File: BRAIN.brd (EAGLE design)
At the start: 125 x 60 mm, 60 parts, among them IC1 ATMEGA328P, IC2 EUP3476SO08T, IC3 RXB1, IC4 TX-C1FLAT, J1 DC_2_1MM, Q1 RJU003N03 N-MOSFET, Q2 RJU003N03 N-MOSFET, Q3 RJU003N03 N-MOSFET, X1 16MHz HC49S

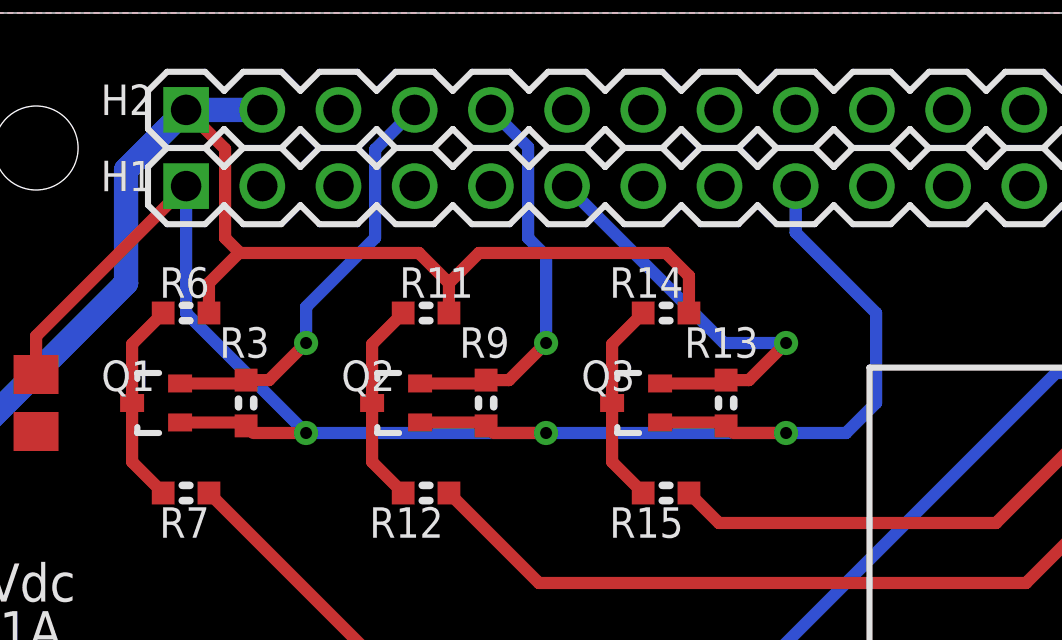
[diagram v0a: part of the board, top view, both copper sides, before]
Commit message: Moved Arduino RESET line from RTS to GPIO4 for manual control
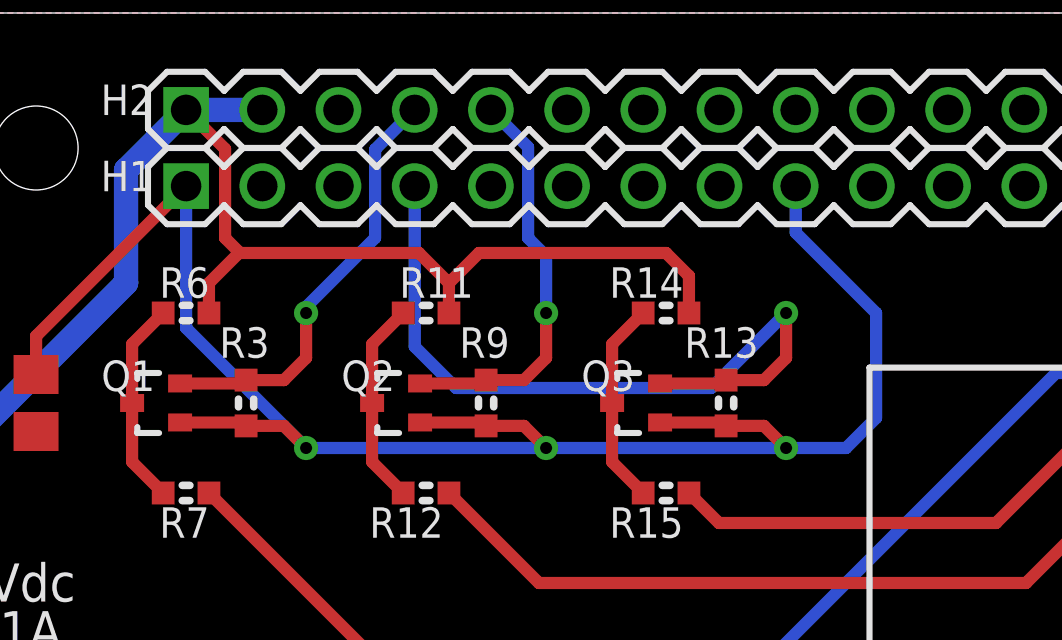
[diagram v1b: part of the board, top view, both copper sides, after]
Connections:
- net GPIO4: now also Q3.2, R13.2
- net PI_RTS: no longer Q3.2, R13.2
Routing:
- net GPIO4: track 0.00 -> 25.5 mm, vias 0 -> 1
- net PI_RTS: track 14.3 -> 0.00 mm, vias 1 -> 0
- net 3.3V: track 59.2 -> 60.8 mm
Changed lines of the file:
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@@
 <layer number="14" name="Route14" color="1" fill="6" visible="no" active="no"/>
 <layer number="15" name="Route15" color="4" fill="6" visible="no" active="no"/>
-<layer number="16" name="Bottom" color="1" fill="1" visible="no" active="yes"/>
+<layer number="16" name="Bottom" color="1" fill="1" visible="yes" active="yes"/>
 <layer number="17" name="Pads" color="2" fill="1" visible="yes" active="yes"/>
-<layer number="18" name="Vias" color="2" fill="1" visible="no" active="yes"/>
+<layer number="18" name="Vias" color="2" fill="1" visible="yes" active="yes"/>
 <layer number="19" name="Unrouted" color="12" fill="1" visible="yes" active="yes"/>
 <layer number="20" name="Dimension" color="15" fill="1" visible="yes" active="yes"/>
@@
 <wire x1="22.8" y1="47.65" x2="25" y2="47.65" width="0.4064" layer="1"/>
 <wire x1="25" y1="47.65" x2="25" y2="47.762" width="0.4064" layer="1"/>
-<wire x1="25" y1="47.762" x2="25.762" y2="47.762" width="0.4064" layer="1"/>
-<wire x1="25.762" y1="47.762" x2="27" y2="49" width="0.4064" layer="1"/>
-<via x="27" y="49" extent="1-16" drill="0.4"/>
+<wire x1="25" y1="47.762" x2="26.262" y2="47.762" width="0.4064" layer="1"/>
+<wire x1="26.262" y1="47.762" x2="27" y2="48.5" width="0.4064" layer="1"/>
+<wire x1="27" y1="48.5" x2="27" y2="50" width="0.4064" layer="1"/>
+<via x="27" y="50" extent="1-16" drill="0.4"/>
 <wire x1="30.62" y1="56.77" x2="29.3" y2="55.45" width="0.4064" layer="16"/>
 <wire x1="29.3" y1="55.45" x2="29.3" y2="52.5" width="0.4064" layer="16"/>
 <wire x1="29.3" y1="52.5" x2="27" y2="50.2" width="0.4064" layer="16"/>
-<wire x1="27" y1="50.2" x2="27" y2="49" width="0.4064" layer="16"/>
+<wire x1="27" y1="50.2" x2="27" y2="50" width="0.4064" layer="16"/>
 </signal>
 <signal name="3.3V">
@@
 <contactref element="H1" pad="1"/>
 <contactref element="H1" pad="9"/>
-<wire x1="25" y1="46.238" x2="25.238" y2="46" width="0.3048" layer="1"/>
-<wire x1="25.238" y1="46" x2="27" y2="46" width="0.4064" layer="1"/>
-<via x="27" y="46" extent="1-16" drill="0.4"/>
-<wire x1="27" y1="46" x2="35" y2="46" width="0.4064" layer="16"/>
-<via x="35" y="46" extent="1-16" drill="0.4"/>
-<wire x1="33" y1="46.238" x2="33.238" y2="46" width="0.3048" layer="1"/>
-<wire x1="33.238" y1="46" x2="35" y2="46" width="0.4064" layer="1"/>
-<wire x1="35" y1="46" x2="43" y2="46" width="0.4064" layer="16"/>
-<via x="43" y="46" extent="1-16" drill="0.4"/>
-<wire x1="43" y1="46" x2="41.238" y2="46" width="0.4064" layer="1"/>
-<wire x1="41.238" y1="46" x2="41" y2="46.238" width="0.3048" layer="1"/>
-<wire x1="23" y1="54.23" x2="23" y2="50" width="0.4064" layer="16"/>
-<wire x1="23" y1="50" x2="27" y2="46" width="0.4064" layer="16"/>
+<via x="27" y="45.5" extent="1-16" drill="0.4"/>
+<wire x1="27" y1="45.5" x2="35" y2="45.5" width="0.4064" layer="16"/>
+<via x="35" y="45.5" extent="1-16" drill="0.4"/>
+<wire x1="35" y1="45.5" x2="43" y2="45.5" width="0.4064" layer="16"/>
+<via x="43" y="45.5" extent="1-16" drill="0.4"/>
+<wire x1="23" y1="54.23" x2="23" y2="49.5" width="0.4064" layer="16"/>
+<wire x1="23" y1="49.5" x2="27" y2="45.5" width="0.4064" layer="16"/>
 <wire x1="18" y1="49.23" x2="23" y2="54.23" width="0.4064" layer="1"/>
 <wire x1="43.32" y1="54.23" x2="43.32" y2="52.68" width="0.4064" layer="16"/>
 <wire x1="43.32" y1="52.68" x2="46" y2="50" width="0.4064" layer="16"/>
-<wire x1="46" y1="50" x2="46" y2="47" width="0.4064" layer="16"/>
-<wire x1="46" y1="47" x2="45" y2="46" width="0.4064" layer="16"/>
-<wire x1="45" y1="46" x2="43" y2="46" width="0.4064" layer="16"/>
+<wire x1="46" y1="50" x2="46" y2="46.5" width="0.4064" layer="16"/>
+<wire x1="46" y1="46.5" x2="45" y2="45.5" width="0.4064" layer="16"/>
+<wire x1="45" y1="45.5" x2="43" y2="45.5" width="0.4064" layer="16"/>
 <contactref element="C3" pad="1"/>
 <wire x1="18" y1="47.95" x2="18" y2="49.23" width="0.4064" layer="1"/>
+<wire x1="25" y1="46.238" x2="26.262" y2="46.238" width="0.4064" layer="1"/>
+<wire x1="26.262" y1="46.238" x2="27" y2="45.5" width="0.4064" layer="1"/>
+<wire x1="33" y1="46.238" x2="34.262" y2="46.238" width="0.4064" layer="1"/>
+<wire x1="34.262" y1="46.238" x2="35" y2="45.5" width="0.4064" layer="1"/>
+<wire x1="41" y1="46.238" x2="42.262" y2="46.238" width="0.4064" layer="1"/>
+<wire x1="42.262" y1="46.238" x2="43" y2="45.5" width="0.4064" layer="1"/>
 </signal>
 <signal name="PI_RX">
@@
 <wire x1="30.8" y1="47.65" x2="33" y2="47.65" width="0.4064" layer="1"/>
 <wire x1="33" y1="47.65" x2="33" y2="47.762" width="0.3048" layer="1"/>
-<wire x1="33" y1="47.762" x2="33.762" y2="47.762" width="0.4064" layer="1"/>
-<wire x1="33.762" y1="47.762" x2="35" y2="49" width="0.4064" layer="1"/>
-<via x="35" y="49" extent="1-16" drill="0.4"/>
+<wire x1="33" y1="47.762" x2="34.262" y2="47.762" width="0.4064" layer="1"/>
+<wire x1="34.262" y1="47.762" x2="35" y2="48.5" width="0.4064" layer="1"/>
+<wire x1="35" y1="48.5" x2="35" y2="50" width="0.4064" layer="1"/>
+<via x="35" y="50" extent="1-16" drill="0.4"/>
 <wire x1="33.16" y1="56.77" x2="34.4" y2="55.53" width="0.4064" layer="16"/>
 <wire x1="34.4" y1="55.53" x2="34.4" y2="52.5" width="0.4064" layer="16"/>
 <wire x1="34.4" y1="52.5" x2="35" y2="51.9" width="0.4064" layer="16"/>
-<wire x1="35" y1="51.9" x2="35" y2="49" width="0.4064" layer="16"/>
+<wire x1="35" y1="51.9" x2="35" y2="50" width="0.4064" layer="16"/>
 </signal>
 <signal name="PI_RTS">
-<contactref element="Q3" pad="2"/>
-<contactref element="R13" pad="2"/>
 <contactref element="H1" pad="6"/>
-<wire x1="38.8" y1="47.65" x2="41" y2="47.65" width="0.4064" layer="1"/>
-<wire x1="41" y1="47.65" x2="41" y2="47.762" width="0.3048" layer="1"/>
-<wire x1="41" y1="47.762" x2="41.762" y2="47.762" width="0.4064" layer="1"/>
-<wire x1="41.762" y1="47.762" x2="43" y2="49" width="0.4064" layer="1"/>
-<via x="43" y="49" extent="1-16" drill="0.4"/>
-<wire x1="43" y1="49" x2="40.93" y2="49" width="0.4064" layer="16"/>
-<wire x1="40.93" y1="49" x2="35.7" y2="54.23" width="0.4064" layer="16"/>
 </signal>
 <signal name="N$2">
@@
 <signal name="GPIO4">
 <contactref element="H1" pad="4"/>
+<contactref element="Q3" pad="2"/>
+<contactref element="R13" pad="2"/>
+<wire x1="38.8" y1="47.65" x2="41" y2="47.65" width="0.4064" layer="1"/>
+<wire x1="41" y1="47.65" x2="41" y2="47.762" width="0.3048" layer="1"/>
+<wire x1="41" y1="47.762" x2="42.262" y2="47.762" width="0.4064" layer="1"/>
+<wire x1="42.262" y1="47.762" x2="43" y2="48.5" width="0.4064" layer="1"/>
+<wire x1="43" y1="48.5" x2="43" y2="50" width="0.4064" layer="1"/>
+<via x="43" y="50" extent="1-16" drill="0.4"/>
+<wire x1="43" y1="50" x2="40.5" y2="47.5" width="0.4064" layer="16"/>
+<wire x1="40.5" y1="47.5" x2="32" y2="47.5" width="0.4064" layer="16"/>
+<wire x1="32" y1="47.5" x2="30.62" y2="48.88" width="0.4064" layer="16"/>
+<wire x1="30.62" y1="48.88" x2="30.62" y2="54.23" width="0.4064" layer="16"/>
 </signal>
 <signal name="GPIO18">

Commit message: Replaced 0805 footprints with 1210
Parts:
- C2, C3: value 10uF 0805 -> 10uF 1210; device freetronics-jon:C0805 -> freetronics-jon:C1210
- moved C2 0.81 mm to (48.5, 14.0)
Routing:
- net 5V: track 306.1 -> 306.6 mm
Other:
- board text added: "(C)2016 SuperHouse Automation P/L"
- board text added: "7-28Vdc"
- board text added: "BLUE"
- board text added: "D0: Serial RX D1: Serial TX D5: RF TX data D6: RF RX LED D7: RF TX LED D8: RF RX data"
- board text added: "GREEN"
- board text added: "YELLOW"
- board text added: "v1.1"
- board text removed: "(C)2015 SuperHouse Automation P/L"
- board text removed: "D0: Serial RX D1: Serial TX D5: RF TX data D6: RF TX LED D7: RF RX LED D8: RF RX data"
- board text removed: "v1.0"
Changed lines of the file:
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@@
 <layer number="19" name="Unrouted" color="12" fill="1" visible="yes" active="yes"/>
 <layer number="20" name="Dimension" color="15" fill="1" visible="yes" active="yes"/>
-<layer number="21" name="tPlace" color="15" fill="1" visible="no" active="yes"/>
-<layer number="22" name="bPlace" color="14" fill="1" visible="no" active="yes"/>
+<layer number="21" name="tPlace" color="15" fill="1" visible="yes" active="yes"/>
+<layer number="22" name="bPlace" color="14" fill="1" visible="yes" active="yes"/>
 <layer number="23" name="tOrigins" color="15" fill="1" visible="yes" active="yes"/>
 <layer number="24" name="bOrigins" color="15" fill="1" visible="yes" active="yes"/>
 <layer number="25" name="tNames" color="7" fill="1" visible="no" active="yes"/>
 <layer number="26" name="bNames" color="7" fill="1" visible="no" active="yes"/>
-<layer number="27" name="tValues" color="7" fill="1" visible="yes" active="yes"/>
+<layer number="27" name="tValues" color="7" fill="1" visible="no" active="yes"/>
 <layer number="28" name="bValues" color="7" fill="1" visible="no" active="yes"/>
 <layer number="29" name="tStop" color="7" fill="3" visible="no" active="yes"/>
@@
 <text x="73.212" y="15.922" size="1.016" layer="21" font="vector" ratio="15">ANT</text>
 <text x="105.811" y="17.668" size="1.016" layer="21" font="vector" ratio="18">POWER</text>
-<text x="67.99" y="4.144" size="1.27" layer="22" ratio="14" rot="MR0">(C)2015 SuperHouse Automation P/L</text>
+<text x="67.99" y="4.144" size="1.27" layer="22" ratio="14" rot="MR0">(C)2016 SuperHouse Automation P/L</text>
 <text x="57.3542" y="24.3216" size="1.27" layer="21" font="vector" ratio="18">RXB6</text>
 <text x="67.558" y="7.026" size="1.27" layer="22" ratio="14" rot="MR0">SKU: BRAIN</text>
@@
 D1: Serial TX
 D5: RF TX data
-D6: RF TX LED
-D7: RF RX LED
+D6: RF RX LED
+D7: RF TX LED
 D8: RF RX data</text>
 <wire x1="64.83" y1="48.18" x2="45.78" y2="48.18" width="0.2032" layer="21"/>
@@
 <wire x1="45.78" y1="32.94" x2="64.83" y2="32.94" width="0.2032" layer="21"/>
 <wire x1="64.83" y1="32.94" x2="64.83" y2="48.18" width="0.2032" layer="21"/>
-<text x="105.811" y="47.668" size="1.016" layer="21" font="vector" ratio="18">RF RX</text>
-<text x="105.811" y="32.668" size="1.016" layer="21" font="vector" ratio="18">RF TX</text>
+<text x="105.811" y="47.668" size="1.016" layer="21" font="vector" ratio="18">RF TX</text>
+<text x="105.811" y="32.668" size="1.016" layer="21" font="vector" ratio="18">RF RX</text>
 <hole x="18" y="6.5" drill="2.8"/>
 <hole x="76" y="6.5" drill="2.8"/>
@@
 <text x="101.5" y="13.0018" size="1.778" layer="22" font="vector" ratio="18" rot="MR90">www.superhouse.tv/brain</text>
 <text x="106.826" y="2.762" size="1.27" layer="22" font="vector" ratio="15" rot="MR0">Reset</text>
-<text x="8.825" y="34.382" size="1.27" layer="22" ratio="18" rot="MR0">9-28Vdc</text>
+<text x="8.825" y="34.382" size="1.27" layer="22" ratio="18" rot="MR0">7-28Vdc</text>
 <text x="8.778" y="32.793" size="1.27" layer="22" ratio="18" rot="MR0">MAX 1A</text>
 <text x="13.425" y="49.082" size="1.27" layer="22" ratio="18" rot="MR0">2.1mm</text>
@@
 <circle x="34" y="23.5" radius="0.3" width="0.4064" layer="21"/>
 <circle x="87" y="37" radius="0.5" width="0.4064" layer="21"/>
-<text x="83" y="5.5" size="1.27" layer="21" ratio="15">v1.0</text>
+<text x="83" y="5.5" size="1.27" layer="21" ratio="15">v1.1</text>
+<text x="105.811" y="41.168" size="1.016" layer="21" font="vector" ratio="18">YELLOW</text>
+<text x="105.811" y="26.168" size="1.016" layer="21" font="vector" ratio="18">GREEN</text>
+<text x="105.811" y="11.168" size="1.016" layer="21" font="vector" ratio="18">BLUE</text>
 </plain>
 <attributes>
@@
 <attribute name="VALUE" x="66.87" y="35.845" size="1.016" layer="27"/>
 </element>
-<element name="C2" library="freetronics-jon" package="C0805" value="10uF 0805" x="49.07" y="14.574" smashed="yes" rot="R90">
-<attribute name="NAME" x="48.304" y="11.2" size="1.016" layer="25"/>
-<attribute name="VALUE" x="44.304" y="11.39" size="1.016" layer="27"/>
-</element>
 <element name="IC1" library="freetronics-master-v1.1" package="TQFP32-08" value="ATMEGA328P" x="91.42" y="32.736" smashed="yes">
 <attribute name="NAME" x="88.245" y="37.816" size="0.4064" layer="25"/>
@@
 </element>
 <element name="S2" library="freetronics-jon" package="TACTILE_SWITCH_SMD_2PIN_TINY" value="RESET" x="104" y="6" smashed="yes" rot="MR180"/>
-<element name="C3" library="freetronics-jon" package="C0805" value="10uF 0805" x="18" y="47" smashed="yes" rot="R270">
-<attribute name="NAME" x="15.23" y="46.77" size="1.016" layer="25"/>
-<attribute name="VALUE" x="17.04" y="43.23" size="1.016" layer="27" rot="R90"/>
-</element>
+<element name="C3" library="freetronics-jon" package="C1210" value="10uF 1210" x="18" y="47" rot="R270"/>
+<element name="C2" library="freetronics-jon" package="C1210" value="10uF 1210" x="48.5" y="14" rot="R90"/>
 </elements>
 <signals>
@@
 <contactref element="IC3" pad="4"/>
 <contactref element="IC4" pad="2"/>
-<contactref element="C2" pad="2"/>
 <contactref element="C10" pad="1"/>
 <contactref element="IC1" pad="4"/>
@@
 <wire x1="101" y1="33" x2="98.5" y2="30.5" width="0.4064" layer="1"/>
 <wire x1="54.67" y1="20.24" x2="54.67" y2="17.59" width="0.4064" layer="1"/>
-<wire x1="49.07" y1="15.524" x2="49.264" y2="15.33" width="0.4064" layer="1"/>
 <wire x1="49.264" y1="15.33" x2="54.93" y2="15.33" width="0.4064" layer="1"/>
 <wire x1="54.93" y1="15.33" x2="54.93" y2="17.33" width="0.4064" layer="1"/>
 <wire x1="54.93" y1="17.33" x2="54.67" y2="17.59" width="0.4064" layer="1"/>
+<contactref element="C2" pad="2"/>
+<wire x1="49.264" y1="15.33" x2="49.194" y2="15.4" width="0.6096" layer="1"/>
+<wire x1="49.194" y1="15.4" x2="48.5" y2="15.4" width="0.6096" layer="1"/>
 </signal>
 <signal name="VIN">
@@
 <contactref element="IC4" pad="4"/>
 <contactref element="IC4" pad="4"/>
-<contactref element="C2" pad="1"/>
 <contactref element="C8" pad="1"/>
 <contactref element="C9" pad="1"/>
@@
 <contactref element="S2" pad="2"/>
 <contactref element="C3" pad="2"/>
+<contactref element="C2" pad="1"/>
 </signal>
 <signal name="N$135">
@@
 <wire x1="23" y1="54.23" x2="23" y2="49.5" width="0.4064" layer="16"/>
 <wire x1="23" y1="49.5" x2="27" y2="45.5" width="0.4064" layer="16"/>
-<wire x1="18" y1="49.23" x2="23" y2="54.23" width="0.4064" layer="1"/>
 <wire x1="43.32" y1="54.23" x2="43.32" y2="52.68" width="0.4064" layer="16"/>
 <wire x1="43.32" y1="52.68" x2="46" y2="50" width="0.4064" layer="16"/>
@@
 <wire x1="46" y1="46.5" x2="45" y2="45.5" width="0.4064" layer="16"/>
 <wire x1="45" y1="45.5" x2="43" y2="45.5" width="0.4064" layer="16"/>
-<contactref element="C3" pad="1"/>
-<wire x1="18" y1="47.95" x2="18" y2="49.23" width="0.4064" layer="1"/>
 <wire x1="25" y1="46.238" x2="26.262" y2="46.238" width="0.4064" layer="1"/>
 <wire x1="26.262" y1="46.238" x2="27" y2="45.5" width="0.4064" layer="1"/>
@@
 <wire x1="41" y1="46.238" x2="42.262" y2="46.238" width="0.4064" layer="1"/>
 <wire x1="42.262" y1="46.238" x2="43" y2="45.5" width="0.4064" layer="1"/>
+<contactref element="C3" pad="1"/>
+<wire x1="23" y1="54.23" x2="23" y2="54" width="0.6096" layer="1"/>
+<wire x1="23" y1="54" x2="21" y2="52" width="0.6096" layer="1"/>
+<wire x1="21" y1="52" x2="20" y2="52" width="0.6096" layer="1"/>
+<wire x1="20" y1="52" x2="18" y2="50" width="0.6096" layer="1"/>
+<wire x1="18" y1="50" x2="18" y2="48.4" width="0.6096" layer="1"/>
 </signal>
 <signal name="PI_RX">
